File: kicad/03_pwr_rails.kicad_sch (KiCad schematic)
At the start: 33 parts, among them U301 TLV62585PDRLR, U311 TLV62585PDRLR, U321 TLV62585PDRLR, U331 TLV62585PDRLR, U341 TLV62585PDRLR

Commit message: Placement with KiCadRoutingTools; Ethernet PHY changed to RTL8211FDI-CG
- Sheet 09 redone for the RTL8211FDI-CG (C692886; the KSZ9031 had 16 orderable, and the
  Agilex 5 card makes the same change). It runs from 3V3 only, with an internal 1.0 V core LDO
  and RGMII pads at 1.8 V from its pad LDO; all nine straps are fitted. PHYRSTB is a 3.3 V
  input, so it is driven through a 74LVC1G07 open drain. The jack LED is driven straight
  from LED2.
- The 1V2 buck (U321) is removed. Power budget and docs updated.
- make_board sets pad pin functions/types, so the placer reads the Y701 oscillator correctly.
- Placement: placement/ holds the inputs (groups, prep, intent fixes, judging chain). Seed 1
  of 12 was chosen by the quick-route judge and applied with tools/apply_placement.py.
  build_pcb.sh no longer rebuilds by default; --rebuild restores the poses.
- tools/jlc: the jlc-tools submodule.

Co-Authored-By: Claude Opus 5.5 <noreply@anthropic.com>
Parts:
- removed C321: 10u, Capacitor_SMD:C_0805_2012Metric, symbol ti135_card:C
- removed C322: 22u, Capacitor_SMD:C_0805_2012Metric, symbol ti135_card:C
- removed L321: 1u, Inductor_SMD:L_Coilcraft_XxL4020, symbol ti135_card:L_Power
- removed R321, R322: 100k, Resistor_SMD:R_0402_1005Metric, symbol ti135_card:R
- removed U321: TLV62585PDRLR, Package_TO_SOT_SMD:SOT-563, symbol ti135_card:TLV62585PDRL
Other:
- note added: "Group 1: 1V8 (VCCAUX, HSIO, LPDDR4 VDD1, eMMC VCCQ, flash), 3V3 (HVIO, eMMC VCC, PHY, translators). Group 2 (EN = pg_group1): 0V85 (DDR PHY VDD_PHY / VDDPLL), 1V1 (DDR VDDQ/VDDQX/VDDQ_CK, LPDDR4 VDD2/VDDQ)."
- note removed: "1V2 KSZ9031 core (group 1)"
- note removed: "Group 1: 1V8 (VCCAUX, HSIO, LPDDR4 VDD1, eMMC VCCQ, flash), 3V3 (HVIO, eMMC VCC, PHY, translators), 1V2 (PHY core). Group 2 (EN = pg_group1): 0V85 (DDR PHY VDD_PHY / VDDPLL), 1V1 (DDR VDDQ/VDDQX/VDDQ_CK, LPDDR4 VDD2/VDDQ)."

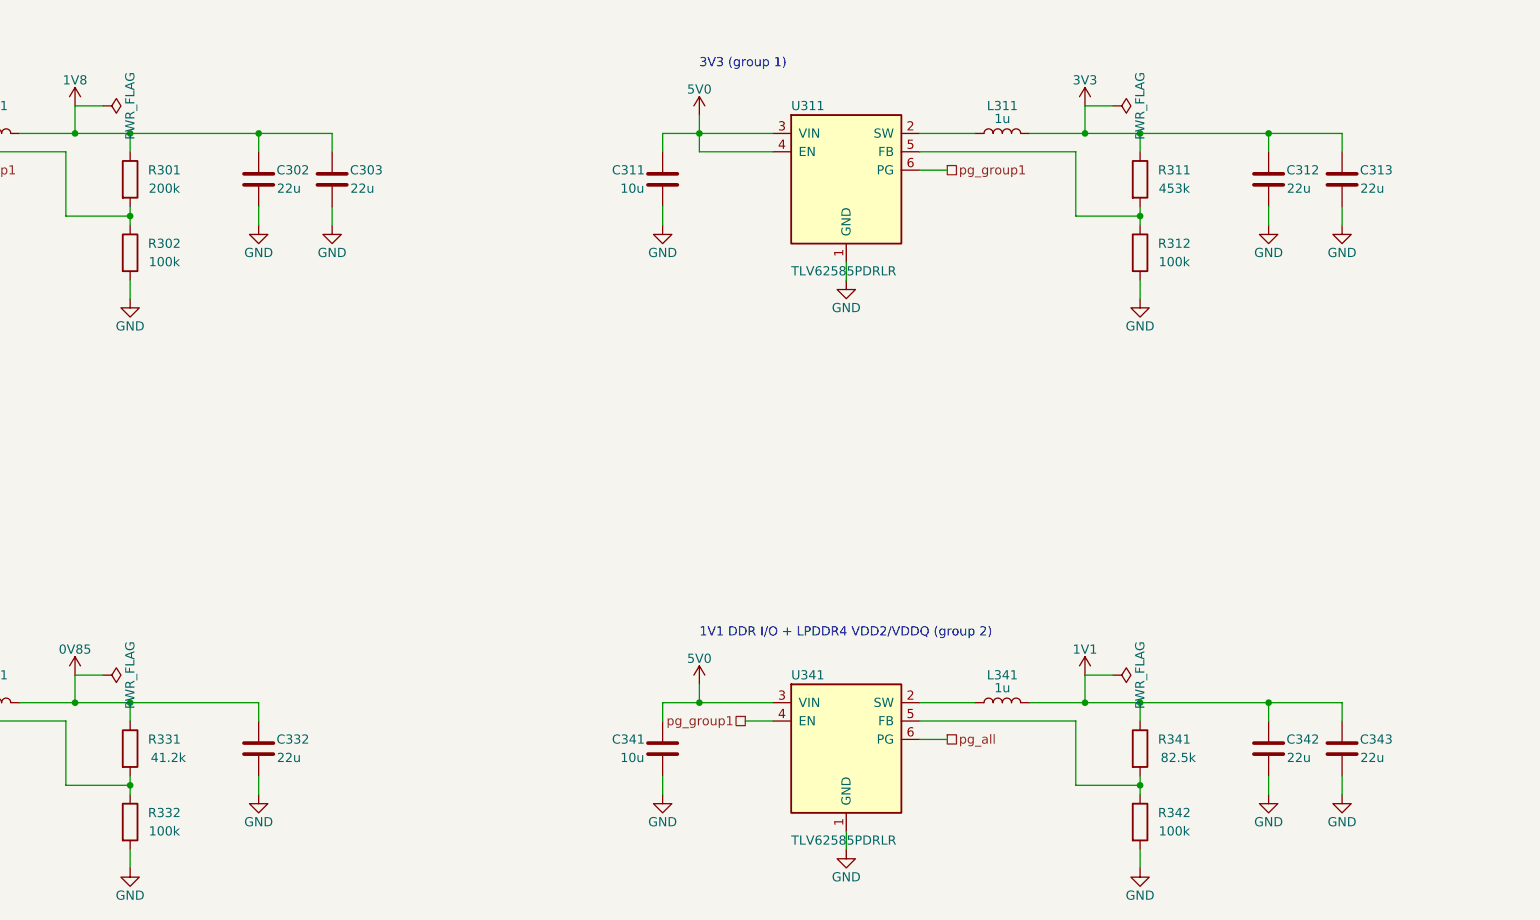
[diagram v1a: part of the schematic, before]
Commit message: Phase 3 (half): checklist fixes in the schematic; board placement still to do
- R801 240R 0.1 % (RT0402BRD07240RL, C852660); SSU_N (L4) 10 k pull-up R622 to 1V8.
- Efinix decoupling table in full on sheet 05 (now A2): C5001-C5073 (0201 10n/1n/100n,
  0402 1u/4u7, 0805 10u/47u, 1206 100u).
- Each TLV62585 cell: 47u output cap and a 22p feed-forward cap across R1 (data sheet:
  feed-forward needed above 47 uF; user decision).
- build_schematic.sh fails on duplicate references (ERC misses them).
- tools/add_parts.py: add missing schematic parts to a routed board; tools/place_free.py
  (untested): nearest free B.Cu spot.
- kicad/ti135_card.kicad_pcb unchanged; placement in work/p3, see NEXT_SESSION.md.

Co-Authored-By: Claude Opus 5.5 <noreply@anthropic.com>
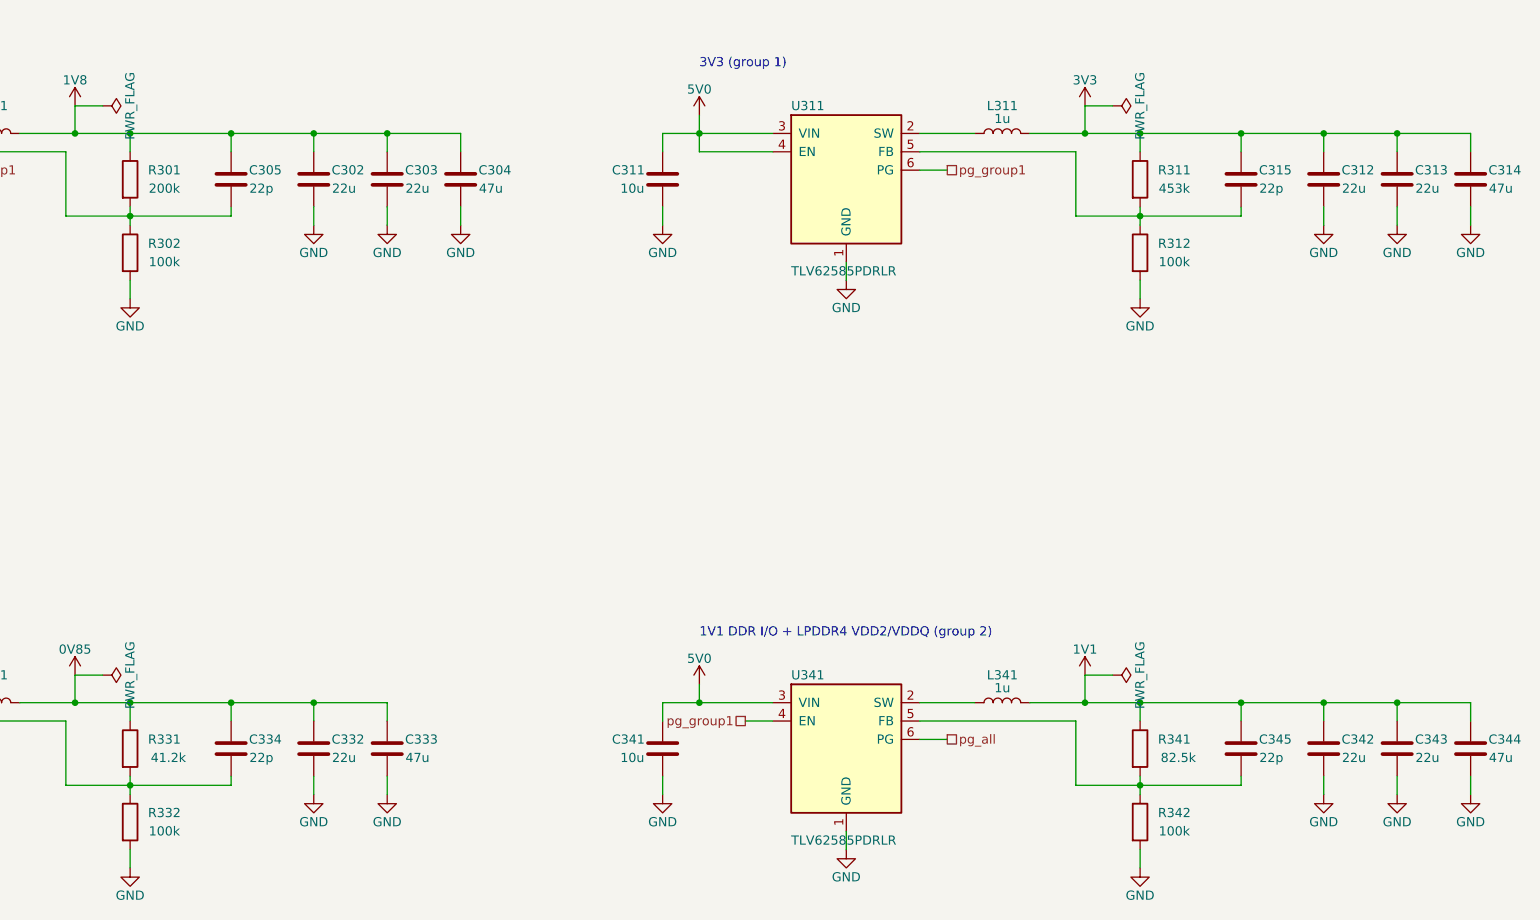
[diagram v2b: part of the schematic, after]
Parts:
- added C304, C314, C333, C344: 47u, Capacitor_SMD:C_0805_2012Metric, symbol ti135_card:C
- added C305, C315, C334, C345: 22p, Capacitor_SMD:C_0402_1005Metric, symbol ti135_card:C
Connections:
- net 0V85: now also C333.1, C334.1
- net 1V1: now also C344.1, C345.1
- net 1V8: now also C304.1, C305.1
- net 3V3: now also C314.1, C315.1
- net GND: now also C304.2, C314.2, C333.2, C344.2
- net at R301.2, R302.1, U301.5 (FB): now also C305.2
- net at R341.2, R342.1, U341.5 (FB): now also C345.2
- net at R331.2, R332.1, U331.5 (FB): now also C334.2
- net at R311.2, R312.1, U311.5 (FB): now also C315.2
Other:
- moved on the sheet: C302, C303, C312, C313, C332, C342, C343

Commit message: LCSC numbers for all JLC parts; Y701 -> YXC OT322525MJBA4SL
- tools/set_lcsc.py: one table (value, footprint) -> LCSC, fills empty LCSC fields in the
  sheets; 312 symbols. JLC basic parts where available, cap voltages checked per rail,
  VCORE divider 0.1 % (no 0.5 % in stock). Board fields synced with add_parts.py.
- Y701: the SiT8924 has no JLC stock; now YXC OT322525MJBA4SL (C669088, 3225), EN tied
  to 1V8. R701/C701 moved 0.5 mm to clear its courtyard. Netlist change: Y701 pin 1 -> 1V8.
- Only U501 (Ti135) is left without LCSC (global sourcing / consigned).
- DRC: schematic parity 0.

Co-Authored-By: Claude Opus 5.5 <noreply@anthropic.com>
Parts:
- C301, C311, C331, C341: LCSC (none) -> C15850
- C302, C303, C312, C313, C332, C342, C343: LCSC (none) -> C45783
- C304, C314, C333, C344: LCSC (none) -> C16780
- C305, C315, C334, C345: LCSC (none) -> C1555
- R301: LCSC (none) -> C25764
- R302, R312, R332, R342: LCSC (none) -> C25741
- R311: LCSC (none) -> C27009
- R331: LCSC (none) -> C26978
- R341: LCSC (none) -> C11717
